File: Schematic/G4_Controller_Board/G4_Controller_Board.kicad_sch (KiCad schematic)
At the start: 48 parts, among them J1 Encoder End, J10 12 Volts In, J11 Preset A, J12 Voltmeter, J13 Preset B, J14 Preset C, J15 Combined Preset Connector, J16 Rev Trigger (Optional), J17 Fire Trigger, J18 Magazine Removal Trigger, J19 Rotary Encoder, J2 Screw_Terminal_01x02, J20 I2C Out, J21 ESC Right, J22 ESC Left, J23 IR LED Rec., J24 IR Led Emitter, J25 IR LED Rec., J26 IR LED Emitter, J3 Preset A, J4 Rev Trigger (Optional), J5 Preset B, J6 Solenoid, J7 Fire Trigger, J8 Preset C, J9 Magazine Removal Trigger, Q1 IRF540N, SW1 Preset A, SW2 Rev Switch, SW3 Preset B, SW4 Fire Switch, SW5 RotaryEncoder_Switch, SW6 Preset C, SW7 MagRemovalSwitch, U1 Mini360, U2 ESP32-LOLIN32-Lite

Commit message: working on software
ported FDL3 software to platformIO (for reference only)
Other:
- note added: "CHECK THIS DIODE: WAS INSTALLED BACKWARDS"
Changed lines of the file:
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@@
+    (effects (font (size 1.27 1.27)) (justify left bottom))
+  )
+  (text "CHECK THIS DIODE: WAS INSTALLED BACKWARDS" (at 63.5 163.83 0)
     (effects (font (size 1.27 1.27)) (justify left bottom))
   )

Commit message: updated controller board schematics
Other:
- note added: "17 = TX2 16 = RX2"
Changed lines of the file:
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@@
+    (effects (font (size 1.27 1.27)) (justify left bottom))
+  )
+  (text "17 = TX2\n16 = RX2" (at 201.93 62.23 0)
     (effects (font (size 1.27 1.27)) (justify left bottom))
   )

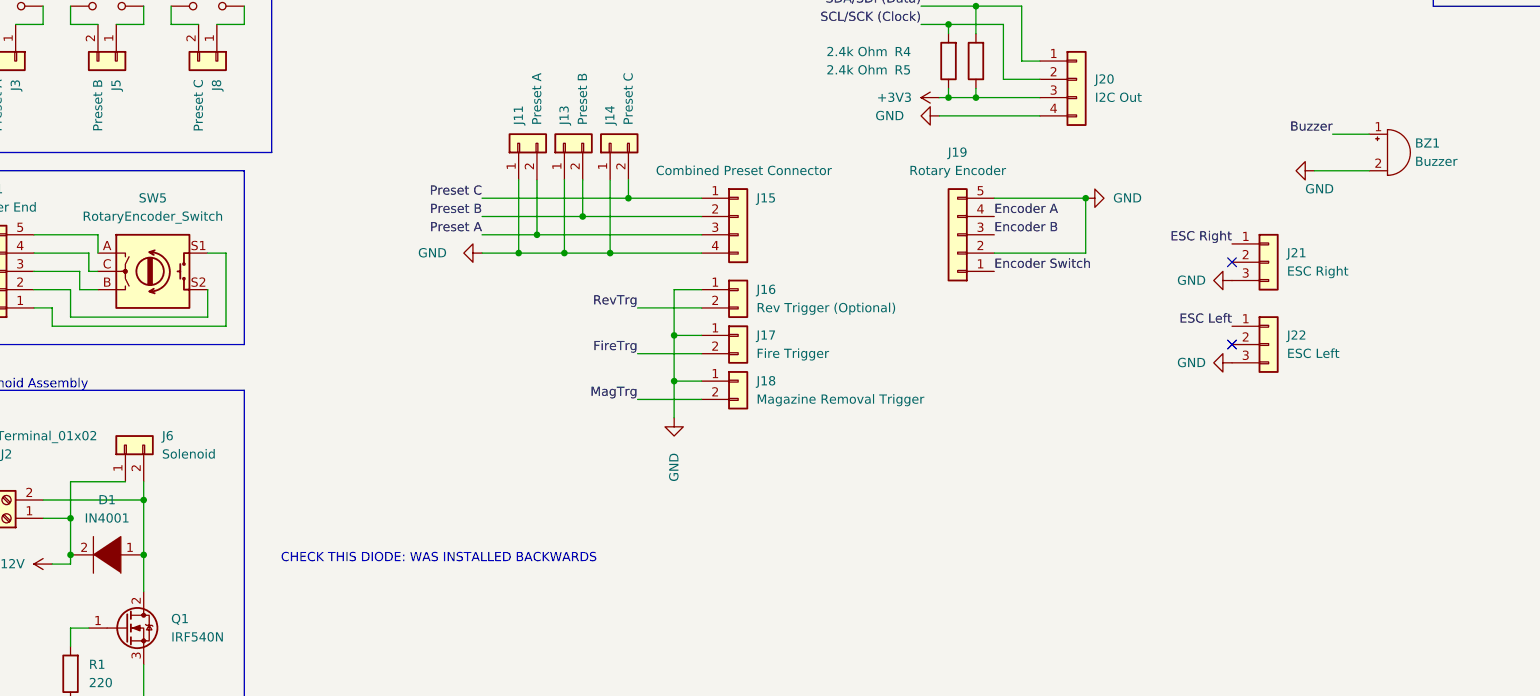
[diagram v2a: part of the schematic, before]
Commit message: work on newer board revision
spitting into 2 boards to make the design both more compact and robust
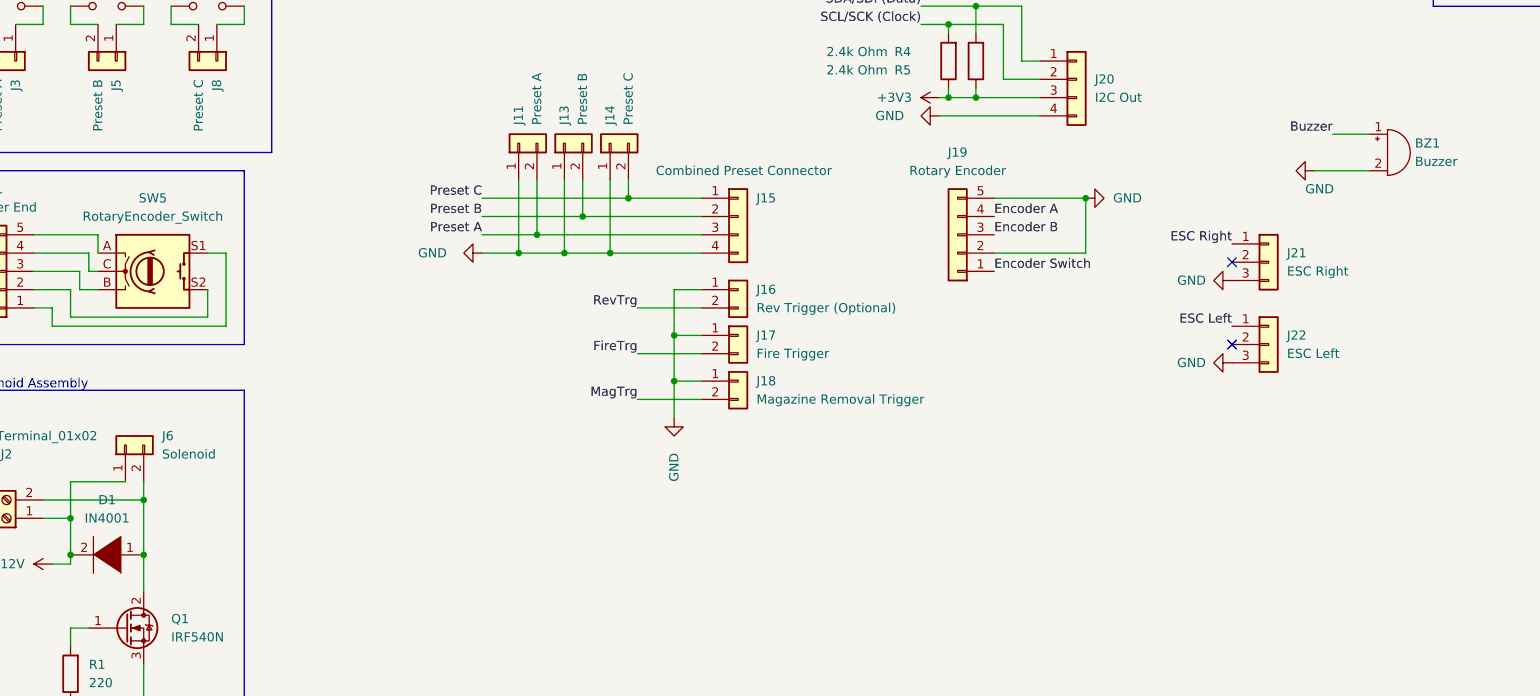
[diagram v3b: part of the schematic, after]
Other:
- note removed: "CHECK THIS DIODE: WAS INSTALLED BACKWARDS"

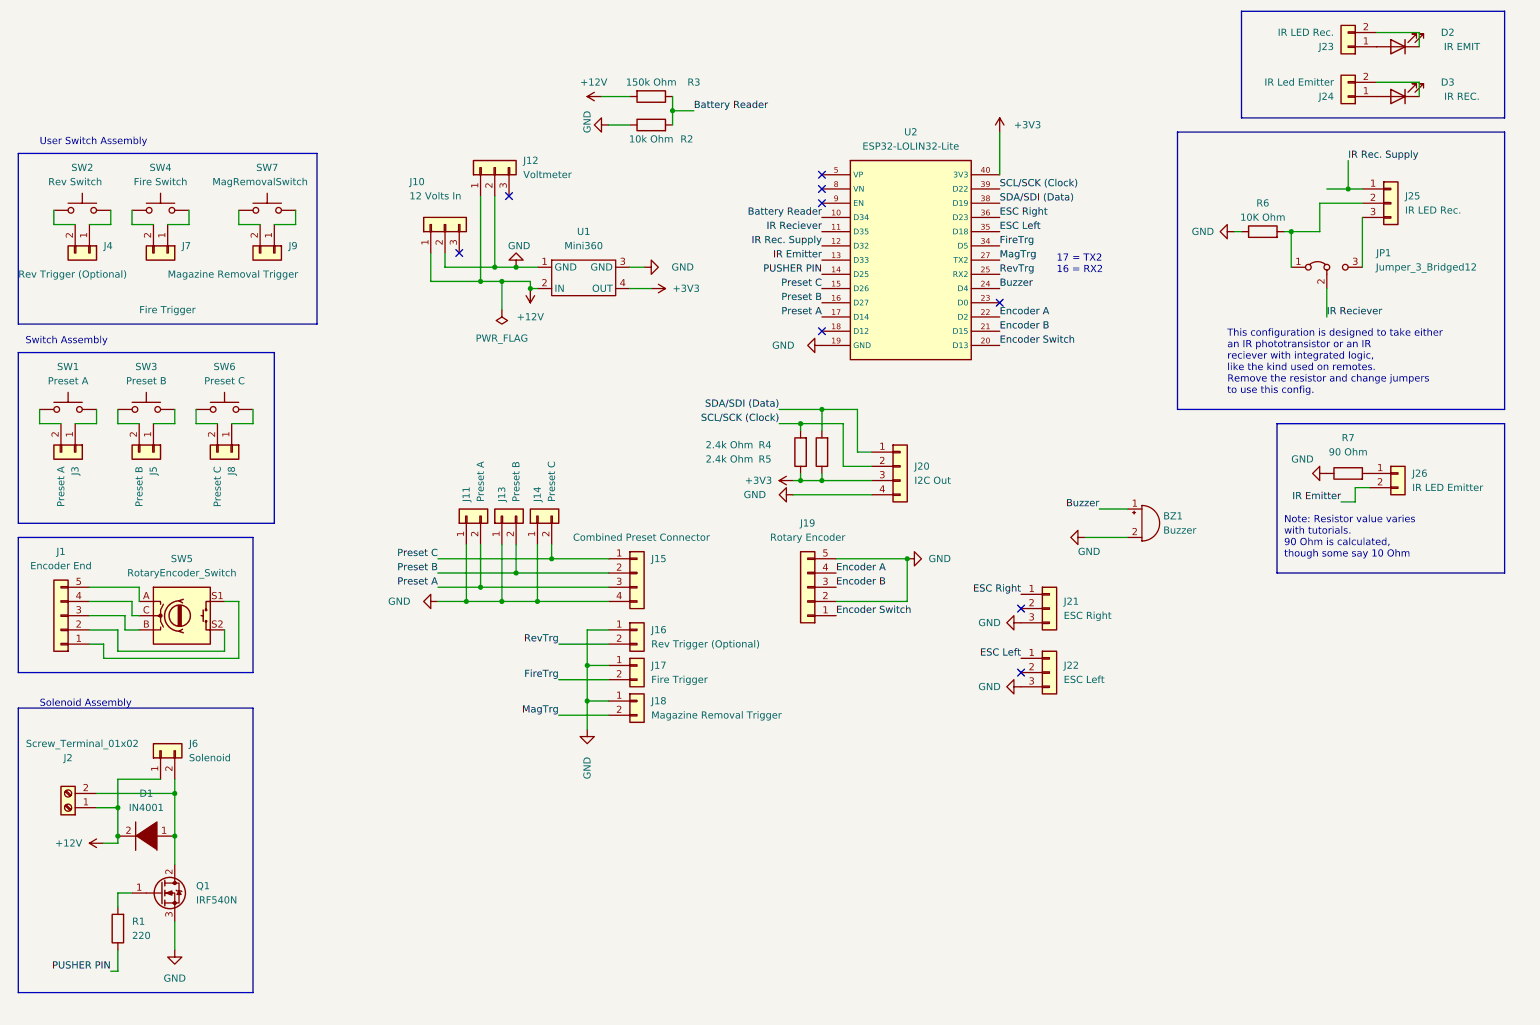
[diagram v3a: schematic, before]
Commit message: begin work on new PCB
2 layers with fast decay driver
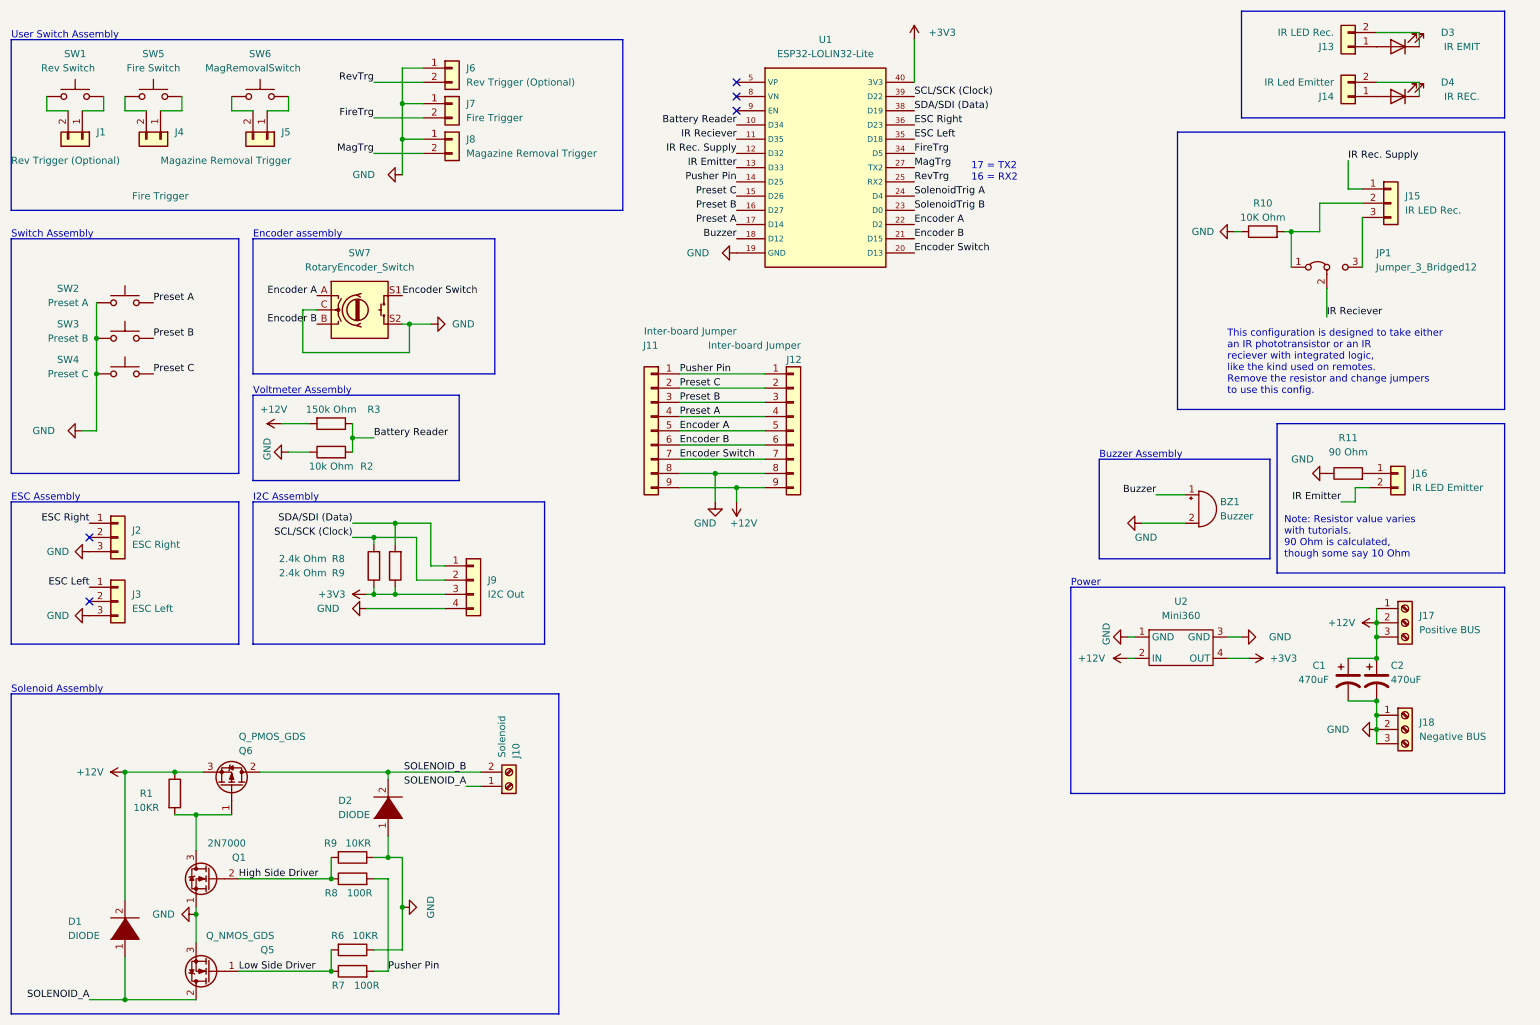
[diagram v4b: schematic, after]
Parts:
- removed J1: Encoder End, Connector_PinSocket_2.54mm:PinSocket_1x05_P2.54mm_Vertical, symbol Connector_Generic:Conn_01x05
- removed J10: 12 Volts In, Connector_PinHeader_2.54mm:PinHeader_1x03_P2.54mm_Vertical, symbol Connector_Generic:Conn_01x03
- removed J11, J3: Preset A, Connector_PinSocket_2.54mm:PinSocket_1x02_P2.54mm_Vertical, symbol Connector_Generic:Conn_01x02
- removed J12: Voltmeter, Connector_PinHeader_2.54mm:PinHeader_1x03_P2.54mm_Vertical, symbol Connector_Generic:Conn_01x03
- removed J13, J5: Preset B, Connector_PinSocket_2.54mm:PinSocket_1x02_P2.54mm_Vertical, symbol Connector_Generic:Conn_01x02
- removed J14, J8: Preset C, Connector_PinSocket_2.54mm:PinSocket_1x02_P2.54mm_Vertical, symbol Connector_Generic:Conn_01x02
- removed J15: Combined Preset Connector, Connector_PinSocket_2.54mm:PinSocket_1x04_P2.54mm_Vertical, symbol Connector_Generic:Conn_01x04
- removed J19: Rotary Encoder, Connector_PinSocket_2.54mm:PinSocket_1x05_P2.54mm_Vertical, symbol Connector_Generic:Conn_01x05
- removed J2: Screw_Terminal_01x02, TerminalBlock_4Ucon:TerminalBlock_4Ucon_1x02_P3.50mm_Horizontal, symbol Connector:Screw_Terminal_01x02
- removed J6: Solenoid, Connector_PinHeader_2.54mm:PinHeader_1x02_P2.54mm_Vertical, symbol Connector_Generic:Conn_01x02
- removed Q1: IRF540N, Package_TO_SOT_THT:TO-220-3_Vertical, symbol Transistor_FET:IRF540N
- added C1, C2: 470uF, Capacitor_THT:CP_Radial_D10.0mm_P5.00mm, symbol Device:C_Polarized_US
- added D2: DIODE, Diode_THT:D_DO-41_SOD81_P7.62mm_Horizontal, symbol pspice:DIODE
- added J10: Solenoid, TerminalBlock_RND:TerminalBlock_RND_205-00001_1x02_P5.00mm_Horizontal, symbol Connector:Screw_Terminal_01x02
- added J11: Inter-board Jumper, Connector_PinHeader_2.54mm:PinHeader_1x09_P2.54mm_Vertical, symbol Connector_Generic:Conn_01x09
- added J12: Inter-board Jumper, Connector_PinSocket_2.54mm:PinSocket_1x09_P2.54mm_Vertical, symbol Connector_Generic:Conn_01x09
- added J17: Positive BUS, TerminalBlock_RND:TerminalBlock_RND_205-00002_1x03_P5.00mm_Horizontal, symbol Connector:Screw_Terminal_01x03
- added J18: Negative BUS, TerminalBlock_RND:TerminalBlock_RND_205-00002_1x03_P5.00mm_Horizontal, symbol Connector:Screw_Terminal_01x03
- added Q1: 2N7000, Package_TO_SOT_THT:TO-92_Inline, symbol Transistor_FET:2N7000
- added Q5: Q_NMOS_GDS, Package_TO_SOT_THT:TO-220-3_Horizontal_TabUp, symbol Device:Q_NMOS_GDS
- added Q6: Q_PMOS_GDS, Package_TO_SOT_THT:TO-220-3_Horizontal_TabUp, symbol Device:Q_PMOS_GDS
- added R6, R9: 10KR, Resistor_THT:R_Axial_DIN0207_L6.3mm_D2.5mm_P7.62mm_Horizontal, symbol Device:R
- added R7, R8: 100R, Resistor_THT:R_Axial_DIN0207_L6.3mm_D2.5mm_P7.62mm_Horizontal, symbol Device:R
- D1: value IN4001 -> DIODE
- R1: value 220 -> 10KR
- SW2: renamed from SW1; footprint (none) -> Button_Switch_THT:SW_PUSH_6mm_H13mm
- SW3: footprint (none) -> Button_Switch_THT:SW_PUSH_6mm_H13mm
- SW4: renamed from SW6; footprint (none) -> Button_Switch_THT:SW_PUSH_6mm_H13mm
- SW7: renamed from SW5; footprint (none) -> Rotary_Encoder:RotaryEncoder_Alps_EC11E-Switch_Vertical_H20mm
- renumbered D2 to D3, D3 to D4, J4 to J1, J23 to J13, J24 to J14, J25 to J15, J26 to J16, J21 to J2, J22 to J3, J7 to J4, J9 to J5, J16 to J6, J17 to J7, J18 to J8, J20 to J9, R6 to R10, R7 to R11, R4 to R8, R5 to R9, SW2 to SW1, SW4 to SW5, SW7 to SW6, U2 to U1, U1 to U2
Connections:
- net +12V: now also R1.1, C1.1, C2.1, J11.9 (Pin_9), J12.9 (Pin_9), J17.1 (Pin_1), J17.2 (Pin_2), J17.3 (Pin_3), Q6.3 (S)
- net Buzzer: now also U1.18 (D12); no longer U1.24 (D4)
- net Encoder A: now also SW7.A, J11.5 (Pin_5), J12.5 (Pin_5)
- net Encoder B: now also SW7.B, J11.6 (Pin_6), J12.6 (Pin_6)
- net Encoder Switch: now also SW7.S1, J11.7 (Pin_7), J12.7 (Pin_7)
- net GND: now also SW2.1, SW3.1, SW4.1, SW7.C, SW7.S2, C1.2, C2.2, D2.1 (K), J11.8 (Pin_8), J12.8 (Pin_8), J18.1 (Pin_1), J18.2 (Pin_2), J18.3 (Pin_3), Q1.1 (S), Q5.3 (S), R6.1, R9.1
- net Preset A: now also SW2.2, J11.4 (Pin_4), J12.4 (Pin_4)
- net Preset B: now also SW3.2, J11.3 (Pin_3), J12.3 (Pin_3)
- net Preset C: now also SW4.2, J11.2 (Pin_2), J12.2 (Pin_2)
- net at R1.2: now also Q1.3 (D), Q6.1 (G)
- net SOLENOID_A: now reaches D1.1 (K)
- net SOLENOID_A: now also J10.1 (Pin_1), Q5.2 (D)
- net SolenoidTrig B: now reaches U1.23 (D0)
- net PUSHER PIN renamed Pusher Pin
- net Pusher Pin: now also J11.1 (Pin_1), J12.1 (Pin_1), R7.2, R8.2; no longer R1.1
- new net High Side Driver: Q1.2 (G), R8.1, R9.2
- new net Low Side Driver: Q5.1 (G), R6.2, R7.1
- new net SOLENOID_B: D2.2 (A), J10.2 (Pin_2), Q6.2 (D)
- new net SolenoidTrig A: U1.24 (D4)
- no-connect marks 9 -> 5
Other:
- note added: "Buzzer Assembly"
- note added: "ESC Assembly"
- note added: "Encoder assembly"
- note added: "I2C Assembly"
- note added: "Power"
- note added: "Voltmeter Assembly"
- title: (none) -> G4 Controller Board
- moved on the sheet: BZ1, J1, J2, J3, J4, J5, J6, J7, J8, J9, R2, R3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

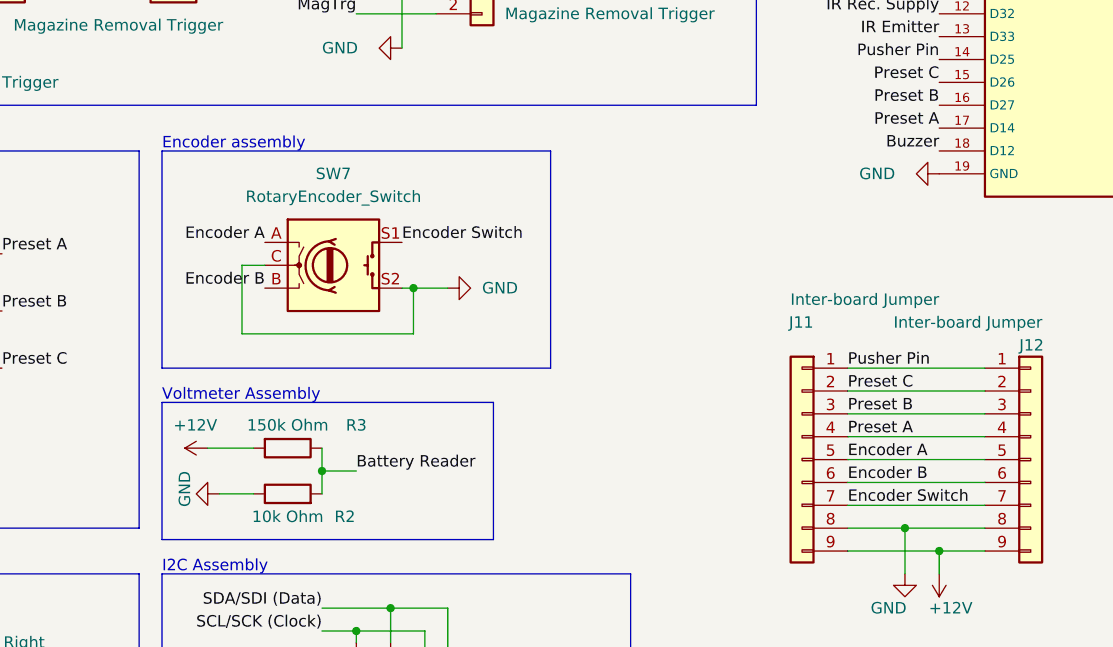
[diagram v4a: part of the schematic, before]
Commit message: update the PCB
added more traces
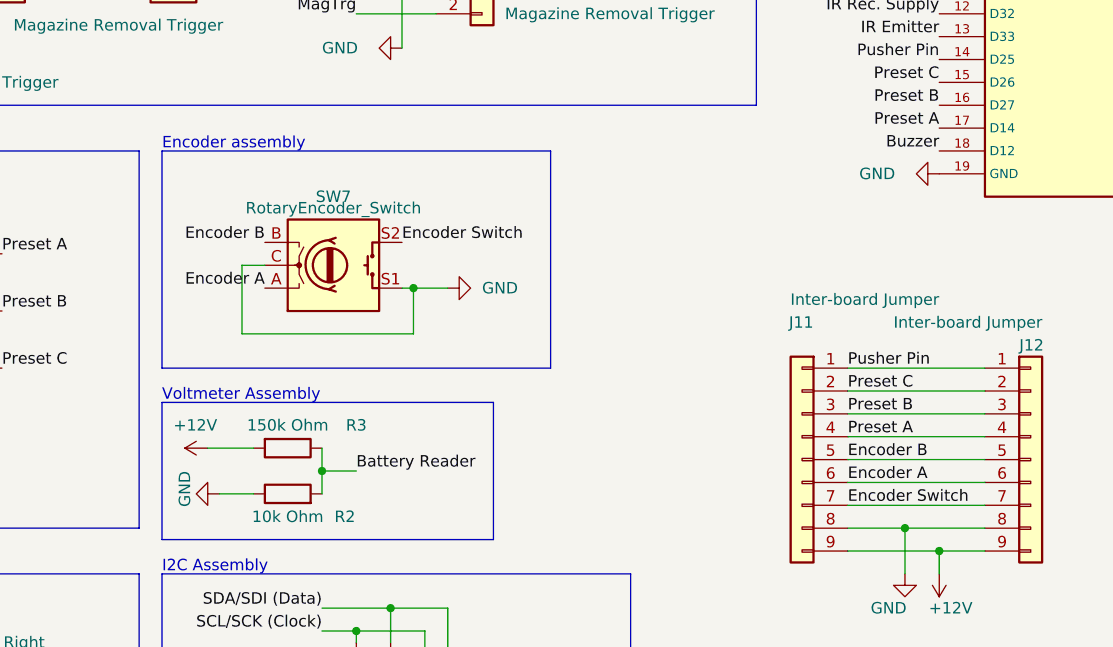
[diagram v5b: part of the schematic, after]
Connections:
- net Encoder A: now also J11.6 (Pin_6), J12.6 (Pin_6); no longer J11.5 (Pin_5), J12.5 (Pin_5)
- net Encoder B: now also J11.5 (Pin_5), J12.5 (Pin_5); no longer J11.6 (Pin_6), J12.6 (Pin_6)
- net Encoder Switch: now also SW7.S2; no longer SW7.S1
- net GND: now also SW7.S1; no longer SW7.S2
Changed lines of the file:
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@@
     (effects (font (size 1.27 1.27)) (justify right bottom))
   )
-  (label "Encoder B" (at 134.62 92.71 0) (fields_autoplaced)
+  (label "Encoder B" (at 134.62 90.17 0) (fields_autoplaced)
     (effects (font (size 1.27 1.27)) (justify left bottom))
   )
@@
     (effects (font (size 1.27 1.27)) (justify left bottom))
   )
-  (label "Encoder A" (at 134.62 90.17 0) (fields_autoplaced)
+  (label "Encoder A" (at 134.62 92.71 0) (fields_autoplaced)
     (effects (font (size 1.27 1.27)) (justify left bottom))
   )
@@
     (effects (font (size 1.27 1.27)) (justify right bottom))
   )
-  (label "Encoder B" (at 69.85 71.12 180) (fields_autoplaced)
+  (label "Encoder B" (at 69.85 66.04 180) (fields_autoplaced)
     (effects (font (size 1.27 1.27)) (justify right bottom))
   )
@@
     (effects (font (size 1.27 1.27)) (justify left bottom))
   )
-  (label "Encoder A" (at 69.85 66.04 180) (fields_autoplaced)
+  (label "Encoder A" (at 69.85 71.12 180) (fields_autoplaced)
     (effects (font (size 1.27 1.27)) (justify right bottom))
   )
@@
     )
   )
-  (symbol (lib_id "Device:RotaryEncoder_Switch") (at 77.47 68.58 0) (unit 1)
-    (in_bom yes) (on_board yes) (dnp no) (fields_autoplaced)
-    (property "Reference" "SW7" (at 77.47 58.42 0)
-      (effects (font (size 1.27 1.27)))
-    )
-    (property "Value" "RotaryEncoder_Switch" (at 77.47 60.96 0)
-      (effects (font (size 1.27 1.27)))
-    )
-    (property "Footprint" "Rotary_Encoder:RotaryEncoder_Alps_EC11E-Switch_Vertical_H20mm" (at 73.66 64.516 0)
-      (effects (font (size 1.27 1.27)) hide)
-    )
-    (property "Datasheet" "~" (at 77.47 61.976 0)
-      (effects (font (size 1.27 1.27)) hide)
-    )
+  (symbol (lib_id "Device:RotaryEncoder_Switch") (at 77.47 68.58 0) (mirror x) (unit 1)
+    (in_bom yes) (on_board yes) (dnp no)
+    (property "Reference" "SW7" (at 77.47 60.96 0)
+      (effects (font (size 1.27 1.27)))
+    )
+    (property "Value" "RotaryEncoder_Switch" (at 77.47 62.23 0)
+      (effects (font (size 1.27 1.27)))
+    )
+    (property "Footprint" "Rotary_Encoder:RotaryEncoder_Alps_EC11E-Switch_Vertical_H20mm" (at 73.66 72.644 0)
+      (effects (font (size 1.27 1.27)) hide)
+    )
+    (property "Datasheet" "~" (at 77.47 75.184 0)
+      (effects (font (size 1.27 1.27)) hide)
+    )
